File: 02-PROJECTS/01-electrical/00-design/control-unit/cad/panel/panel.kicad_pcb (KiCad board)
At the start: 2 copper layers, 180 x 84.8 mm, 56 parts, among them J1 panel ribbon 2x13 IDC, keyed, J2 screen module I2C 4-pin, J3 plate header 2x6 IDC, keyed (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, SW1 key - rear defog, SW2 key - HVAC mode, SW3 key - recirculate, SW4 key - mirror defog, SW5 window DRV, SW6 window PASS, SW7 encoder - centre, SW8 encoder - driver seat, SW9 encoder - passenger seat, U2 IS31FL3236A-TQLS4

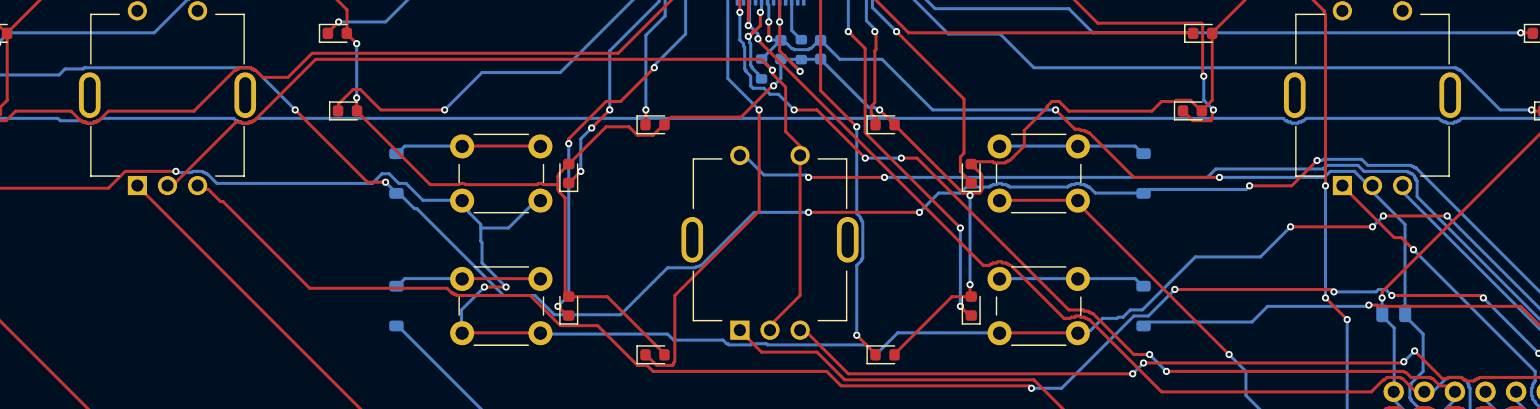
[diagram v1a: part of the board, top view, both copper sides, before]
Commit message: Electrical: the independent read's findings fixed on the boards before the order, and the Display Unit's brake-warning input given its pull-up (D-549)
Y44 done; Y18 (the board order) opens. DU carrier rev 0.06: road-speed input IC08 re-laid, a 15 V gate zener and 4.7 k on the backlight switch, four vias at each backlight layer change, brake warning IC06 pulled up to 3V3 (found while the changes were read back - it could never have read high), tell-tale dividers 22 k, MMBT5551 and SL310A on the rails clamped at 53 V. CU carrier rev 0.07, values only: C27 100 nF, Q1 / Q2 SQ2364EES, Q4 MMBT5551, D1 SL310A. Panel: the encoders' lug slots to Bourns' layout. Two assembly drawings in each fab folder in place of silkscreen references.

ERC 0, DRC 0 / 0 / 0, check.py 0 mismatches on all five boards. The DU carrier's and the panel's fab zips are rebuilt under the same names; the CU carrier's and the upper board's are unchanged. Cart 98 lines. Record: icu_channels IC06 IC08 IC09 IC12 IC13, dcu_channels SN23 SN24, parts P106 P107 P147 P149 P169 P170 P203, Y18 / F3 / F5 briefs and steps. D-548's DT13 question is untouched (V-117).

Co-Authored-By: Claude Opus 5.5 <noreply@anthropic.com>
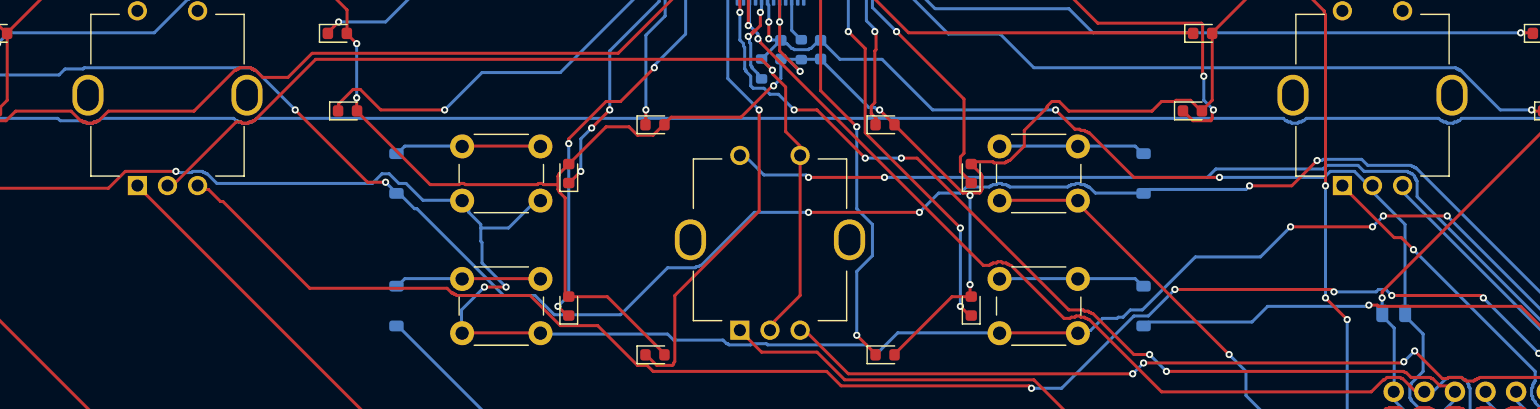
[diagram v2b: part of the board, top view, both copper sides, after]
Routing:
- net /LR3: track 33.0 -> 33.7 mm
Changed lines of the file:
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@@
 		)
 		(pad "MP" thru_hole oval
-			(at -6.45 0)
-			(size 1.8 3.8)
-			(drill oval 1 3)
+			(at -6.6 0)
+			(size 2.6 3.4)
+			(drill oval 1.8 2.6)
 			(layers "*.Cu" "*.Mask")
 			(remove_unused_layers no)
 		)
 		(pad "MP" thru_hole oval
-			(at 6.45 0)
-			(size 1.8 3.8)
-			(drill oval 1 3)
+			(at 6.6 0)
+			(size 2.6 3.4)
+			(drill oval 1.8 2.6)
 			(layers "*.Cu" "*.Mask")
 			(remove_unused_layers no)
@@
 		)
 		(pad "MP" thru_hole oval
-			(at -6.45 0)
-			(size 1.8 3.8)
-			(drill oval 1 3)
+			(at -6.6 0)
+			(size 2.6 3.4)
+			(drill oval 1.8 2.6)
 			(layers "*.Cu" "*.Mask")
 			(remove_unused_layers no)
 		)
 		(pad "MP" thru_hole oval
-			(at 6.45 0)
-			(size 1.8 3.8)
-			(drill oval 1 3)
+			(at 6.6 0)
+			(size 2.6 3.4)
+			(drill oval 1.8 2.6)
 			(layers "*.Cu" "*.Mask")
 			(remove_unused_layers no)
@@
 		)
 		(pad "MP" thru_hole oval
-			(at -6.45 0)
-			(size 1.8 3.8)
-			(drill oval 1 3)
+			(at -6.6 0)
+			(size 2.6 3.4)
+			(drill oval 1.8 2.6)
 			(layers "*.Cu" "*.Mask")
 			(remove_unused_layers no)
 		)
 		(pad "MP" thru_hole oval
-			(at 6.45 0)
-			(size 1.8 3.8)
-			(drill oval 1 3)
+			(at 6.6 0)
+			(size 2.6 3.4)
+			(drill oval 1.8 2.6)
 			(layers "*.Cu" "*.Mask")
 			(remove_unused_layers no)
@@
 	(segment
 		(start 97.2 62.3)
-		(end 97.2 56.5)
+		(end 97.2 57)
 		(width 0.25)
 		(layer "B.Cu")
@@
 	)
 	(segment
-		(start 97.2 52.2)
+		(start 97.2 51.8)
 		(end 97.2 45)
 		(width 0.25)
@@
 	)
 	(segment
-		(start 97.6 56.1)
-		(end 97.6 56)
+		(start 98.5 55.7)
+		(end 98.5 53.1)
 		(width 0.25)
 		(layer "B.Cu")
@@
 	)
 	(segment
-		(start 97.6 52.7)
-		(end 97.5 52.6)
-		(width 0.25)
-		(layer "B.Cu")
-		(net "/LR3")
-	)
-	(segment
-		(start 97.2 56.5)
-		(end 97.6 56.1)
+		(start 98.5 53.1)
+		(end 97.2 51.8)
 		(width 0.25)
 		(layer "B.Cu")
@@
 	)
 	(segment
-		(start 97.7 55.9)
-		(end 97.7 52.9)
-		(width 0.25)
-		(layer "B.Cu")
-		(net "/LR3")
-	)
-	(segment
-		(start 97.5 52.6)
-		(end 97.5 52.5)
-		(width 0.25)
-		(layer "B.Cu")
-		(net "/LR3")
-	)
-	(segment
-		(start 97.6 52.8)
-		(end 97.6 52.7)
-		(width 0.25)
-		(layer "B.Cu")
-		(net "/LR3")
-	)
-	(segment
-		(start 97.5 52.5)
-		(end 97.2 52.2)
-		(width 0.25)
-		(layer "B.Cu")
-		(net "/LR3")
-	)
-	(segment
-		(start 97.7 52.9)
-		(end 97.6 52.8)
-		(width 0.25)
-		(layer "B.Cu")
-		(net "/LR3")
-	)
-	(segment
-		(start 97.6 56)
-		(end 97.7 55.9)
+		(start 97.2 57)
+		(end 98.5 55.7)
 		(width 0.25)
 		(layer "B.Cu")

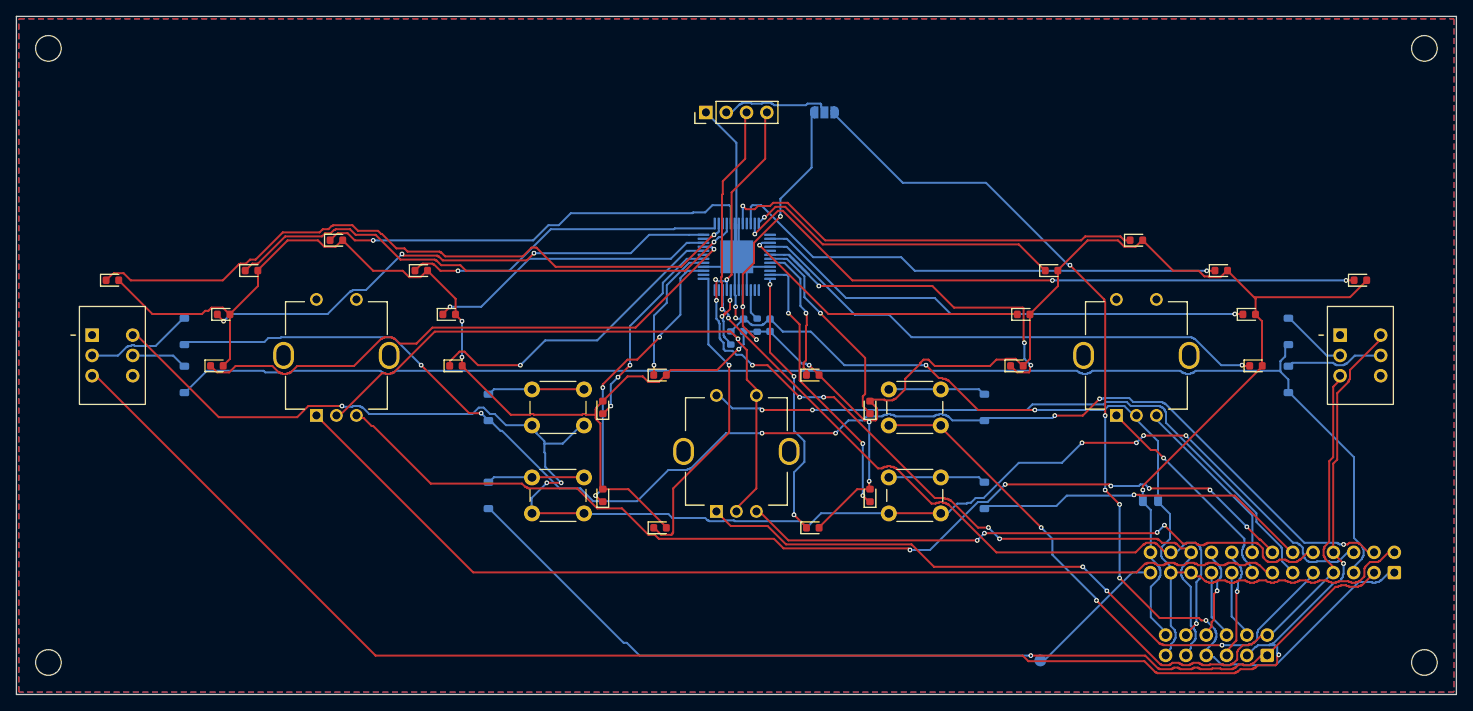
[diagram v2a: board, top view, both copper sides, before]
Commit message: Electrical: the panel board redrawn for the single-DIN face, 180 x 47.3 (D-582)
Y55. Rev 0.05: every part moved up by the mock-up's crop (board y =
sketch y - 4.5), the ribbon and plate headers to the top edge, the screen
header, jumper, test point, holes and two ring lights moved onto the
board; re-routed by freerouting with GND as a signal and the pours
refilled, U2 pin 41 hand-finished. DRC 0 / 0 / 0 with parity; check.py
panel 79 / 0 and left-plate 29 / 0, its plate rule now DP-DCU 36-47.
Fab zip, assembly drawings and STEP rebuilt; the scene places the board
again. Y18's brief and step take the new size; P175 follows.

Co-Authored-By: Claude Opus 5.5 <noreply@anthropic.com>
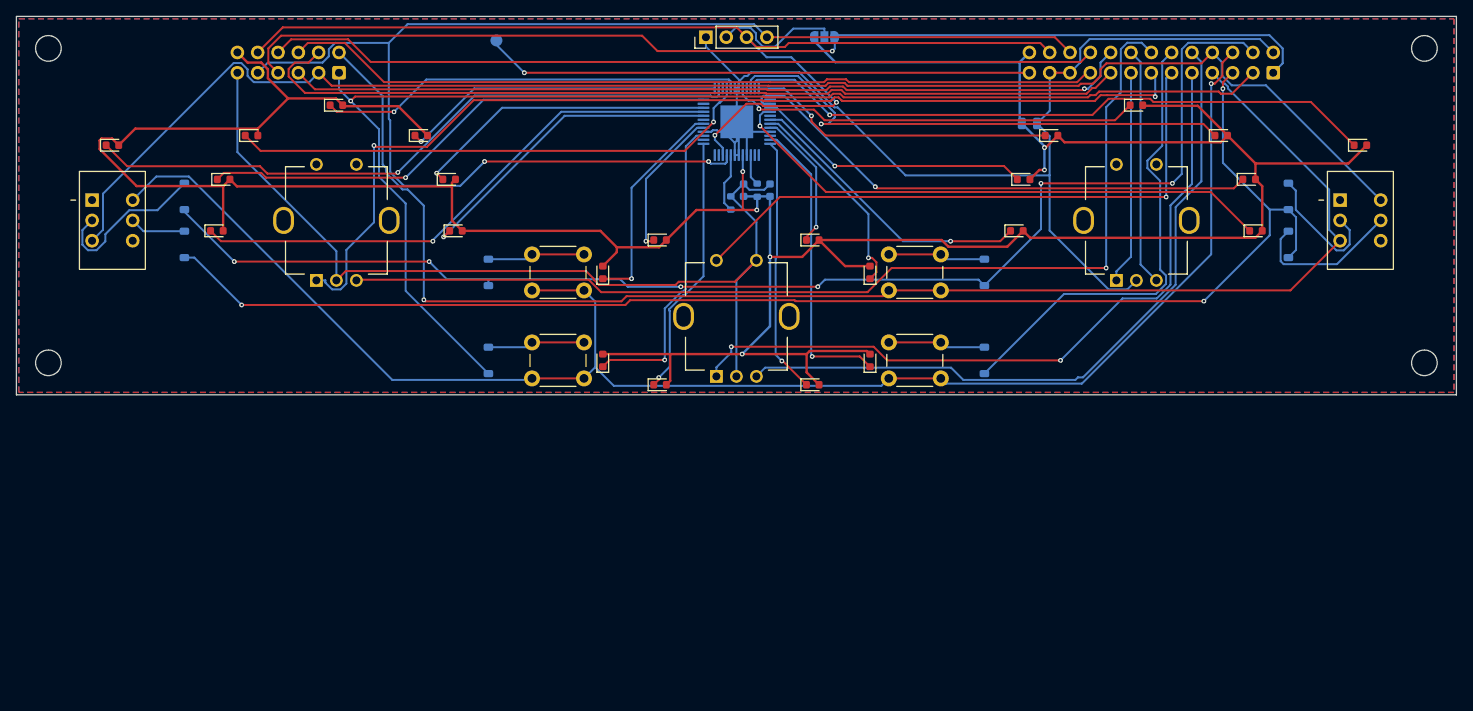
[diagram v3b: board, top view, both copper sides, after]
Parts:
- moved J3 137.0 mm to (40.3, 7.04)
- moved TP1 103.1 mm to (60.0, 3.00)
- moved J1 64.3 mm to (157.1, 7.04)
- moved C1 49.5 mm to (126.6, 13.4)
- moved H3 37.5 mm to (4.00, 43.3)
- moved H4 37.5 mm to (176.0, 43.3)
- moved LED7 17.9 mm to (99.5, 46.0)
- moved LED8 17.9 mm to (80.5, 46.0)
- moved LED13 16.9 mm to (25.1, 26.8)
- moved LED18 16.9 mm to (54.9, 26.8)
- moved LED19 16.9 mm to (125.1, 26.8)
- moved LED24 16.9 mm to (154.9, 26.8)
- moved R1 16.9 mm to (89.3, 23.3)
- moved C2 16.9 mm to (94.2, 21.7)
- moved C3 16.9 mm to (90.9, 21.7)
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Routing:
- net /JOY_X: track 6.96 -> 110.7 mm
- net /+5V_PNL: track 320.6 -> 417.5 mm, vias 10 -> 6
- net /JOY_PRESS: track 6.92 -> 102.3 mm
- net /AGND: track 9.88 -> 103.9 mm, vias 1 -> 0
- net /JOY_Y: track 12.5 -> 105.8 mm
- net /COL2: track 94.5 -> 181.2 mm, vias 2 -> 1
- net /PNL_SDA: track 114.6 -> 167.4 mm, vias 8 -> 2
- net /SPARE: track 16.8 -> 68.6 mm, vias 0 -> 1
- net /ROW1: track 121.8 -> 160.3 mm
- net GND: track 226.6 -> 259.6 mm, vias 5 -> 0
- net /COL3: track 212.6 -> 186.7 mm, vias 2 -> 0
- net /PNL_SCL: track 111.7 -> 136.7 mm, vias 3 -> 2
- net /COL1: track 181.0 -> 198.8 mm, vias 7 -> 1
- net /ROW4: track 40.9 -> 58.5 mm, vias 1 -> 0
- net /ENC_CENTRE_B: track 73.8 -> 89.3 mm, vias 4 -> 0
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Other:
- board size 180 x 84.8 mm -> 180 x 47.3 mm
